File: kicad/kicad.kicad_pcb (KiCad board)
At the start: 2 copper layers, 22 parts, among them SW1 SW_PUSH, SW10 SW_PUSH, SW11 SW_PUSH, SW12 SW_PUSH, SW13 SW_PUSH, SW14 SW_PUSH, SW15 SW_PUSH, SW16 SW_PUSH, SW17 SW_PUSH, SW2 SW_PUSH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

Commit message: fixed schema and drew traces
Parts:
- PROG1: moved to B.Cu
- moved PROG1 9.35 mm to (104.5, 121.1)
- moved SW2 0.07 mm to (100.0, 90.0)
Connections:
- PROG1 pad 3: DIOL -> CLKL
- YJT1 pad 2: SW34L -> SW24L
- YJT1 pad 20: SW20L -> SW00L
- YJT1 pad 22: SW00L -> SW20L
- YJT1 pad 3: SW33L -> SW14L
- YJT1 pad 34: unconnected-(YJT1-Pad34) -> SW33L
- YJT1 pad 35: unconnected-(YJT1-Pad35) -> SW34L
- YJT1 pad 4: SW24L -> SW04L
- YJT1 pad 5: SW14L -> unconnected-(YJT1-Pad5)
- YJT1 pad 6: SW04L -> unconnected-(YJT1-Pad6)
- YJT2 pad 15: SW00L -> SW20L
- YJT2 pad 17: SW20L -> SW00L
- YJT2 pad 2: unconnected-(YJT2-Pad2) -> SW34L
- YJT2 pad 29: SW04L -> unconnected-(YJT2-Pad29)
- YJT2 pad 3: unconnected-(YJT2-Pad3) -> SW33L
- YJT2 pad 30: SW14L -> unconnected-(YJT2-Pad30)
- YJT2 pad 33: SW24L -> SW04L
- YJT2 pad 34: SW33L -> SW14L
- YJT2 pad 35: SW34L -> SW24L
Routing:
- net SW00L: track 0.00 -> 93.1 mm, vias 0 -> 1
- net VCC: track 0.00 -> 91.8 mm, vias 0 -> 3
- net SW01L: track 0.00 -> 88.4 mm, vias 0 -> 1
- net SW02L: track 0.00 -> 76.3 mm, vias 0 -> 1
- net SW10L: track 0.00 -> 74.1 mm, vias 0 -> 1
- net SW04L: track 0.00 -> 72.2 mm, vias 0 -> 1
- net SW11L: track 0.00 -> 70.6 mm, vias 0 -> 1
- net DIOL: track 0.00 -> 64.3 mm, vias 0 -> 1
- net SW20L: track 0.00 -> 64.1 mm, vias 0 -> 1
- net CLKL: track 0.00 -> 63.3 mm, vias 0 -> 1
- net SW34L: track 0.00 -> 60.9 mm, vias 0 -> 1
- net SW03L: track 0.00 -> 59.9 mm, vias 0 -> 1
- net SW12L: track 0.00 -> 59.0 mm, vias 0 -> 1
- net SW14L: track 0.00 -> 56.7 mm, vias 0 -> 1
- net SW21L: track 0.00 -> 50.3 mm, vias 0 -> 1
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
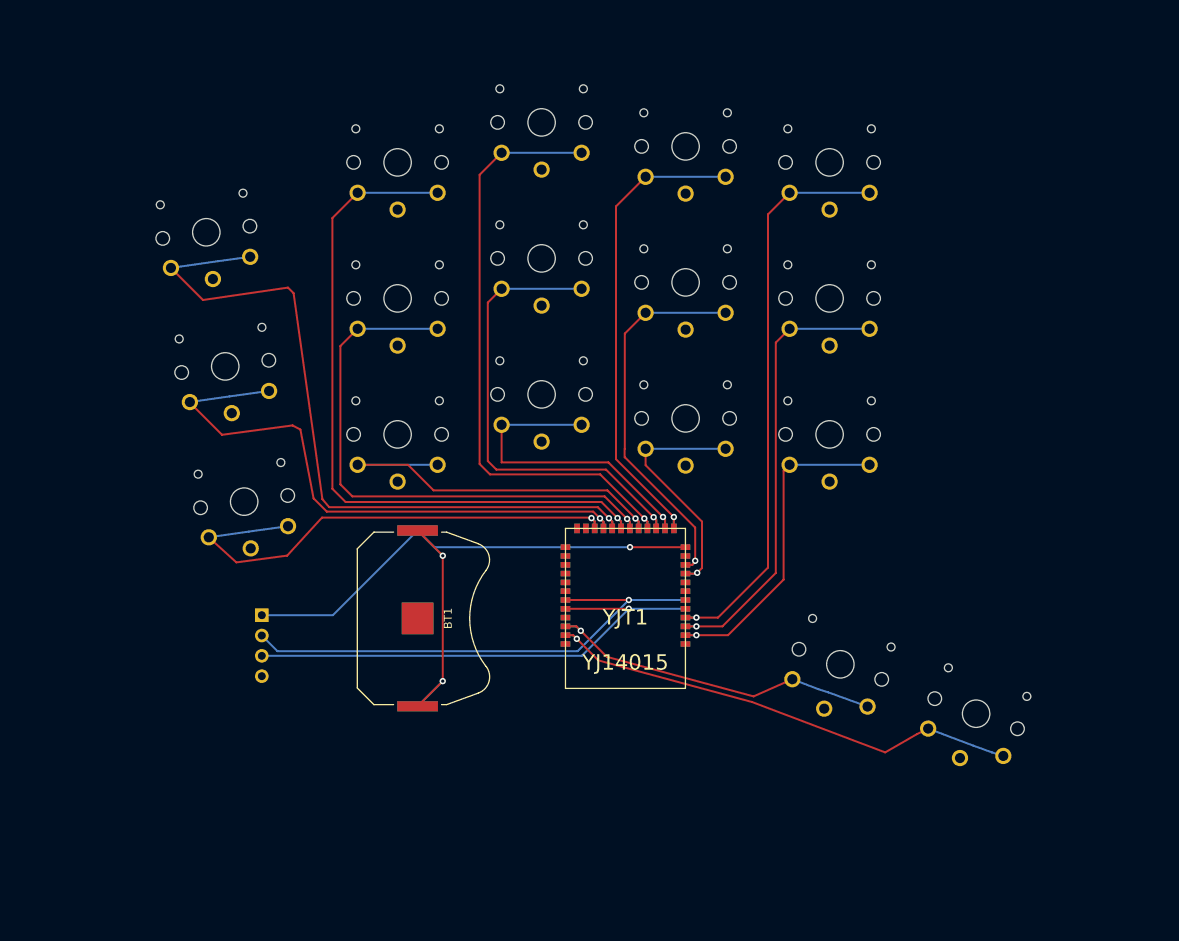
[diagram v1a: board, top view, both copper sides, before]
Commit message: Added outline and made it look nicer
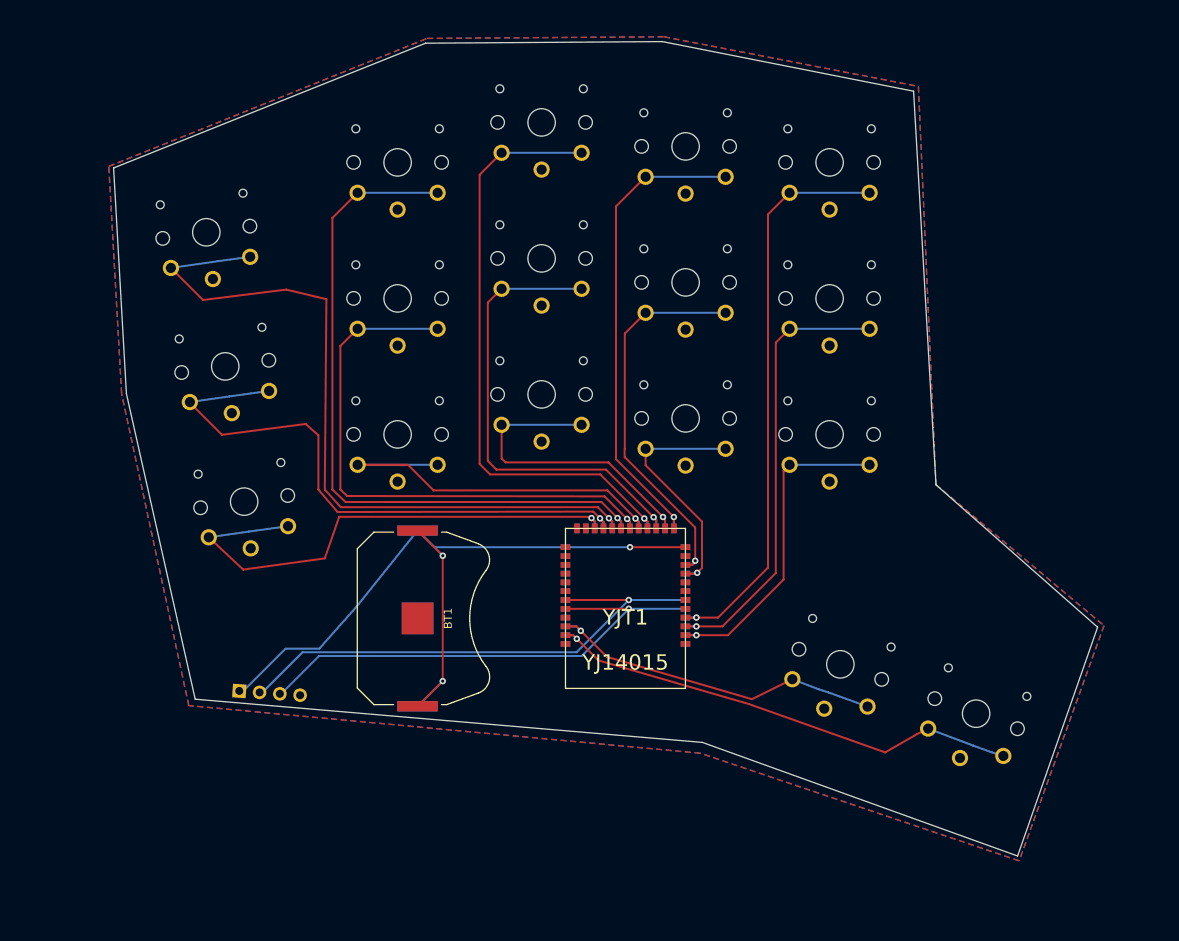
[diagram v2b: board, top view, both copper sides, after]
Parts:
- moved PROG1 9.88 mm to (101.7, 130.6), turned to -94 degrees
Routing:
- net VCC: track 91.8 -> 99.6 mm
- net SW20L: track 64.1 -> 66.2 mm
- net SW00L: track 93.1 -> 95.1 mm
- net DIOL: track 64.3 -> 66.1 mm
- net SW10L: track 74.1 -> 74.8 mm
- added copper zone on B.Cu, net GND
- added copper zone on F.Cu, net GND
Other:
- board outline added: 123 x 101.8 mm

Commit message: Updated shape
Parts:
- moved PROG1 6.49 mm to (100.7, 124.2), turned to -114 degrees
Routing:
- net CLKL: track 63.1 -> 66.5 mm
- net DIOL: track 66.1 -> 68.8 mm
- net SW14L: track 56.7 -> 54.8 mm
- net SW34L: track 60.8 -> 62.6 mm
- net SW33L: track 43.4 -> 45.1 mm
- net SW00L: track 95.1 -> 93.4 mm
- net SW21L: track 50.3 -> 52.0 mm
- net SW04L: track 72.2 -> 70.7 mm
- net VCC: track 99.6 -> 98.0 mm
- net SW22L: track 40.5 -> 41.9 mm
- net SW24L: track 41.2 -> 40.1 mm
- net SW12L: track 59.0 -> 59.5 mm
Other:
- board size 123 x 101.8 mm -> 121.6 x 100 mm

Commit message: Made things look nicer
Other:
- board size 121.6 x 100 mm -> 119.7 x 98.8 mm
- board text added: "CLKL"
- board text added: "DIOL"
- board text added: "GND"
- board text added: "VCC"
- board text added: "gurt-portable v0.1"
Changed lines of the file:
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@@
     )
   )
-  (gr_line (start 198 150.2) (end 160.4 137) (layer "Edge.Cuts") (width 0.1))
-  (gr_line (start 167 55.4) (end 184.8 55.6) (layer "Edge.Cuts") (width 0.1))
-  (gr_line (start 86.6 65.4) (end 105.4 62.8) (layer "Edge.Cuts") (width 0.1))
-  (gr_line (start 94.6 122.6) (end 86.6 65.4) (layer "Edge.Cuts") (width 0.1))
-  (gr_line (start 118.8 134) (end 98 125.6) (layer "Edge.Cuts") (width 0.1))
-  (gr_line (start 149 53.4) (end 167 53.4) (layer "Edge.Cuts") (width 0.1))
-  (gr_line (start 98 125.6) (end 94.6 122.6) (layer "Edge.Cuts") (width 0.1))
-  (gr_line (start 129.8 50.2) (end 149 50.4) (layer "Edge.Cuts") (width 0.1))
-  (gr_line (start 129.8 55) (end 129.8 50.2) (layer "Edge.Cuts") (width 0.1))
-  (gr_line (start 112 55.2) (end 129.8 55) (layer "Edge.Cuts") (width 0.1))
-  (gr_line (start 208.2 122.2) (end 198 150.2) (layer "Edge.Cuts") (width 0.1))
-  (gr_line (start 167 53.4) (end 167 55.4) (layer "Edge.Cuts") (width 0.1))
-  (gr_line (start 185 113.6) (end 208.2 122.2) (layer "Edge.Cuts") (width 0.1))
-  (gr_line (start 105.4 62.8) (end 112 55.2) (layer "Edge.Cuts") (width 0.1))
-  (gr_line (start 160.4 137) (end 118.8 134) (layer "Edge.Cuts") (width 0.1))
-  (gr_line (start 184.8 55.6) (end 185 113.6) (layer "Edge.Cuts") (width 0.1))
-  (gr_line (start 149 50.4) (end 149 53.4) (layer "Edge.Cuts") (width 0.1))
+  (gr_line (start 197 149.52) (end 161.87 136.93) (layer "Edge.Cuts") (width 0.1))
+  (gr_arc (start 167.75 55.75) (mid 167.042893 55.457107) (end 166.75 54.75) (layer "Edge.Cuts") (width 0.1))
+  (gr_arc (start 95.89 123.77) (mid 95.393079 123.365506) (end 95.15 122.77) (layer "Edge.Cuts") (width 0.1))
+  (gr_line (start 167.75 55.75) (end 183.85 55.8) (layer "Edge.Cuts") (width 0.1))
+  (gr_arc (start 130.207107 51.757107) (mid 130.5 51.05) (end 131.207107 50.757107) (layer "Edge.Cuts") (width 0.1))
+  (gr_line (start 87.97 65.77) (end 111.27 62.48) (layer "Edge.Cuts") (width 0.1))
+  (gr_arc (start 159.94 136.44) (mid 160.929303 136.590798) (end 161.87 136.93) (layer "Edge.Cuts") (width 0.1))
+  (gr_line (start 95.15 122.77) (end 87.31 66.68) (layer "Edge.Cuts") (width 0.1))
+  (gr_line (start 117.49 133.41) (end 95.89 123.77) (layer "Edge.Cuts") (width 0.1))
+  (gr_line (start 149.74 53.75) (end 165.75 53.7) (layer "Edge.Cuts") (width 0.1))
+  (gr_line (start 131.207107 50.757107) (end 147.75 50.74) (layer "Edge.Cuts") (width 0.1))
+  (gr_arc (start 206.487564 123.743336) (mid 206.951962 124.11948) (end 206.94 124.716229) (layer "Edge.Cuts") (width 0.1))
+  (gr_line (start 130.21 54.76) (end 130.207107 51.757107) (layer "Edge.Cuts") (width 0.1))
+  (gr_line (start 113.297107 55.797107) (end 129.21 55.76) (layer "Edge.Cuts") (width 0.1))
+  (gr_arc (start 112.27 61.48) (mid 111.928717 62.138717) (end 111.27 62.48) (layer "Edge.Cuts") (width 0.1))
+  (gr_arc (start 147.75 50.74) (mid 148.457107 51.032893) (end 148.75 51.74) (layer "Edge.Cuts") (width 0.1))
+  (gr_arc (start 130.21 54.76) (mid 129.917107 55.467107) (end 129.21 55.76) (layer "Edge.Cuts") (width 0.1))
+  (gr_line (start 206.94 124.716229) (end 198.04 149.12) (layer "Edge.Cuts") (width 0.1))
+  (gr_arc (start 198.04 149.12) (mid 197.590409 149.503063) (end 197 149.52) (layer "Edge.Cuts") (width 0.1))
+  (gr_line (start 185.753439 116.26) (end 206.487564 123.743336) (layer "Edge.Cuts") (width 0.1))
+  (gr_arc (start 112.297107 56.797107) (mid 112.59 56.09) (end 113.297107 55.797107) (layer "Edge.Cuts") (width 0.1))
+  (gr_line (start 112.27 61.48) (end 112.297107 56.797107) (layer "Edge.Cuts") (width 0.1))
+  (gr_line (start 159.94 136.44) (end 119.344297 134.03625) (layer "Edge.Cuts") (width 0.1))
+  (gr_arc (start 165.75 53.7) (mid 166.475 54.010714) (end 166.75 54.75) (layer "Edge.Cuts") (width 0.1))
+  (gr_arc (start 185.753439 116.26) (mid 185.189688 115.80262) (end 185.013439 115.096802) (layer "Edge.Cuts") (width 0.1))
+  (gr_line (start 184.85 56.8) (end 185.013439 115.096802) (layer "Edge.Cuts") (width 0.1))
+  (gr_arc (start 149.74 53.75) (mid 149.032893 53.457107) (end 148.74 52.75) (layer "Edge.Cuts") (width 0.1))
+  (gr_arc (start 183.85 55.8) (mid 184.557107 56.092893) (end 184.85 56.8) (layer "Edge.Cuts") (width 0.1))
+  (gr_line (start 148.75 51.74) (end 148.74 52.75) (layer "Edge.Cuts") (width 0.1))
+  (gr_arc (start 119.344297 134.03625) (mid 118.389634 133.803632) (end 117.49 133.41) (layer "Edge.Cuts") (width 0.1))
+  (gr_arc (start 87.31 66.68) (mid 87.446287 66.087189) (end 87.97 65.77) (layer "Edge.Cuts") (width 0.1))
+  (gr_text "gurt-portable v0.1" (at 146.9 132.75 -3) (layer "B.SilkS")
+    (effects (font (size 1.5 1.5) (thickness 0.3)) (justify mirror))
+  )
+  (gr_text "DIOL" (at 104.15 122.6 68) (layer "B.SilkS")
+    (effects (font (size 1 1) (thickness 0.15)) (justify mirror))
+  )
+  (gr_text "GND" (at 108.8 124.8 68) (layer "B.SilkS")
+    (effects (font (size 1 1) (thickness 0.15)) (justify mirror))
+  )
+  (gr_text "VCC" (at 101.75 121.8 67) (layer "B.SilkS")
+    (effects (font (size 1 1) (thickness 0.15)) (justify mirror))
+  )
+  (gr_text "CLKL" (at 106.55 123.4 68) (layer "B.SilkS")
+    (effects (font (size 1 1) (thickness 0.15)) (justify mirror))
+  )
+  (gr_text "gurt-portable v0.1" (at 146.9 132.85 -3) (layer "F.SilkS")
+    (effects (font (size 1.5 1.5) (thickness 0.3)))
+  )
+  (gr_text "CLKL" (at 106.51254 123.492718 68) (layer "F.SilkS")
+    (effects (font (size 1 1) (thickness 0.15)))
+  )
+  (gr_text "VCC" (at 101.75 121.8 67) (layer "F.SilkS")
+    (effects (font (size 1 1) (thickness 0.15)))
+  )
+  (gr_text "DIOL" (at 104.131268 122.64636 68) (layer "F.SilkS")
+    (effects (font (size 1 1) (thickness 0.15)))
+  )
+  (gr_text "GND" (at 108.84636 124.81873 68) (layer "F.SilkS")
+    (effects (font (size 1 1) (thickness 0.15)))
+  )
   (segment (start 127.15 113.665) (end 124 110.515) (width 0.25) (layer "F.Cu") (net 1))
   (segment (start 127.1425 129.3425) (end 127.1425 113.6725) (width 0.25) (layer "F.Cu") (net 1))

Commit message: fixed ordere
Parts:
- turned BT1 to 0 degrees
- turned BT2 to 180 degrees
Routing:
- net VCC: track 98.0 -> 76.6 mm
- net CLKL: track 66.5 -> 62.8 mm
- net DIOL: track 68.8 -> 65.6 mm
